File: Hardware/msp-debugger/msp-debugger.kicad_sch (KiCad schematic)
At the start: 18 parts, among them J1 USB_B_Micro, J2 Conn_02x10, J3 Conn_02x10, J4 Conn_01x04_Pin, U1 MSP430G2553IN20, U2 NHD-0420H1Z, U3 BA033CC0FP-E2, U4 FT230XS-R

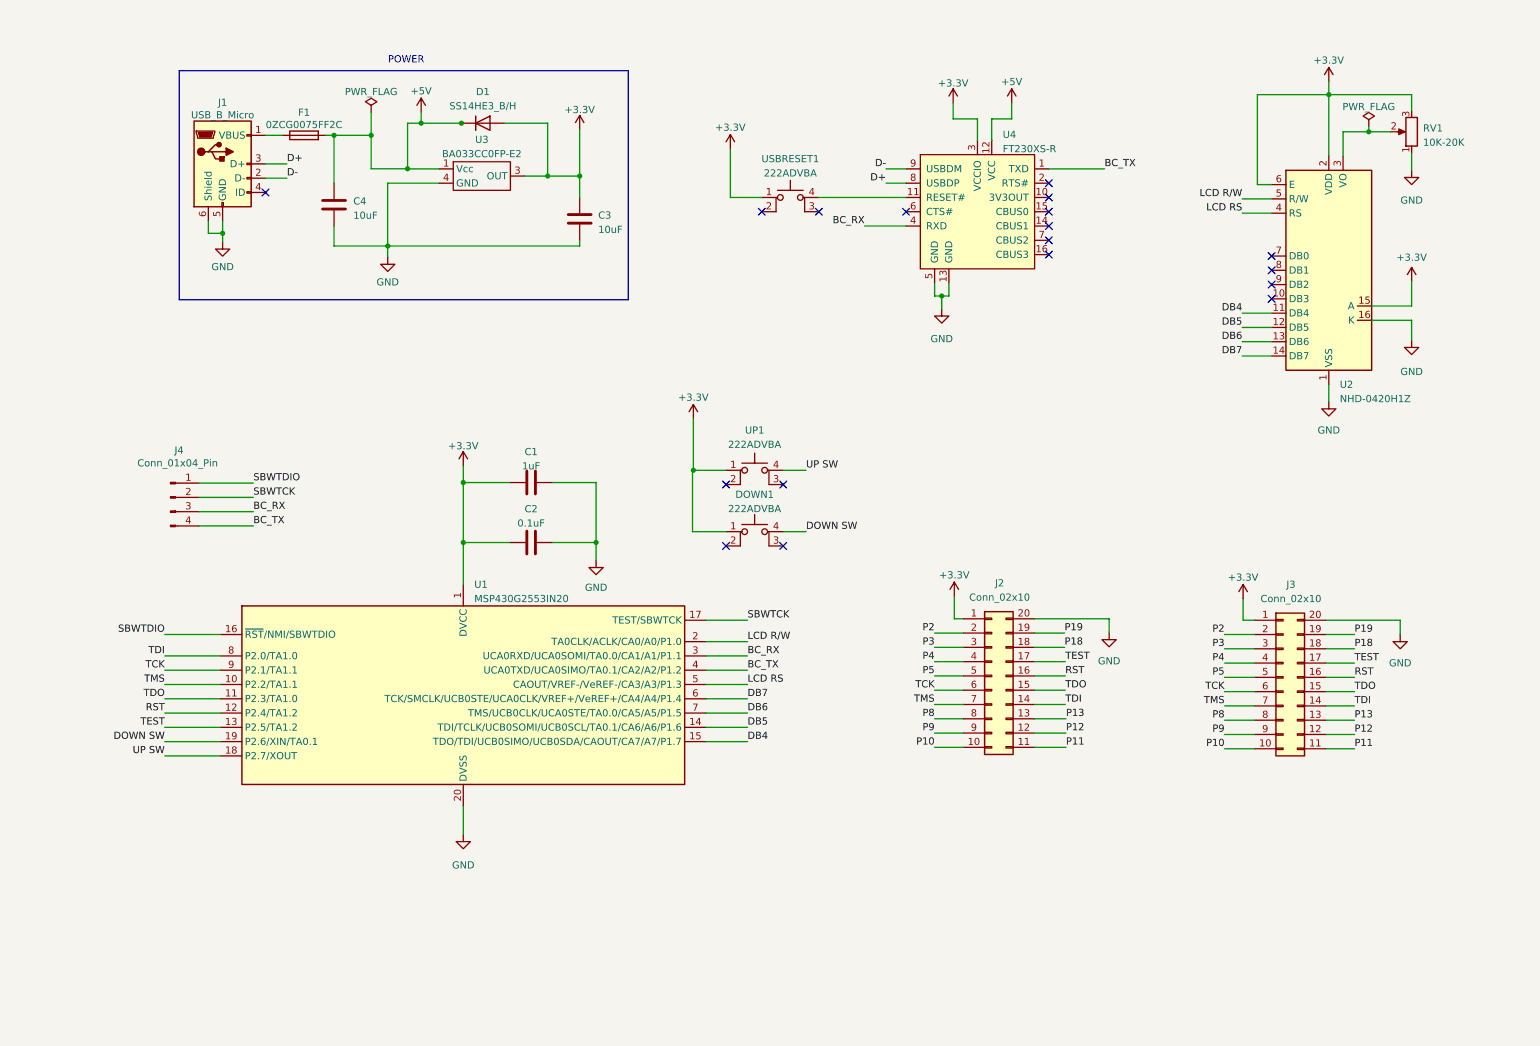
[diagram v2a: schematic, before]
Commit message: update schematic to use length 40 lcd
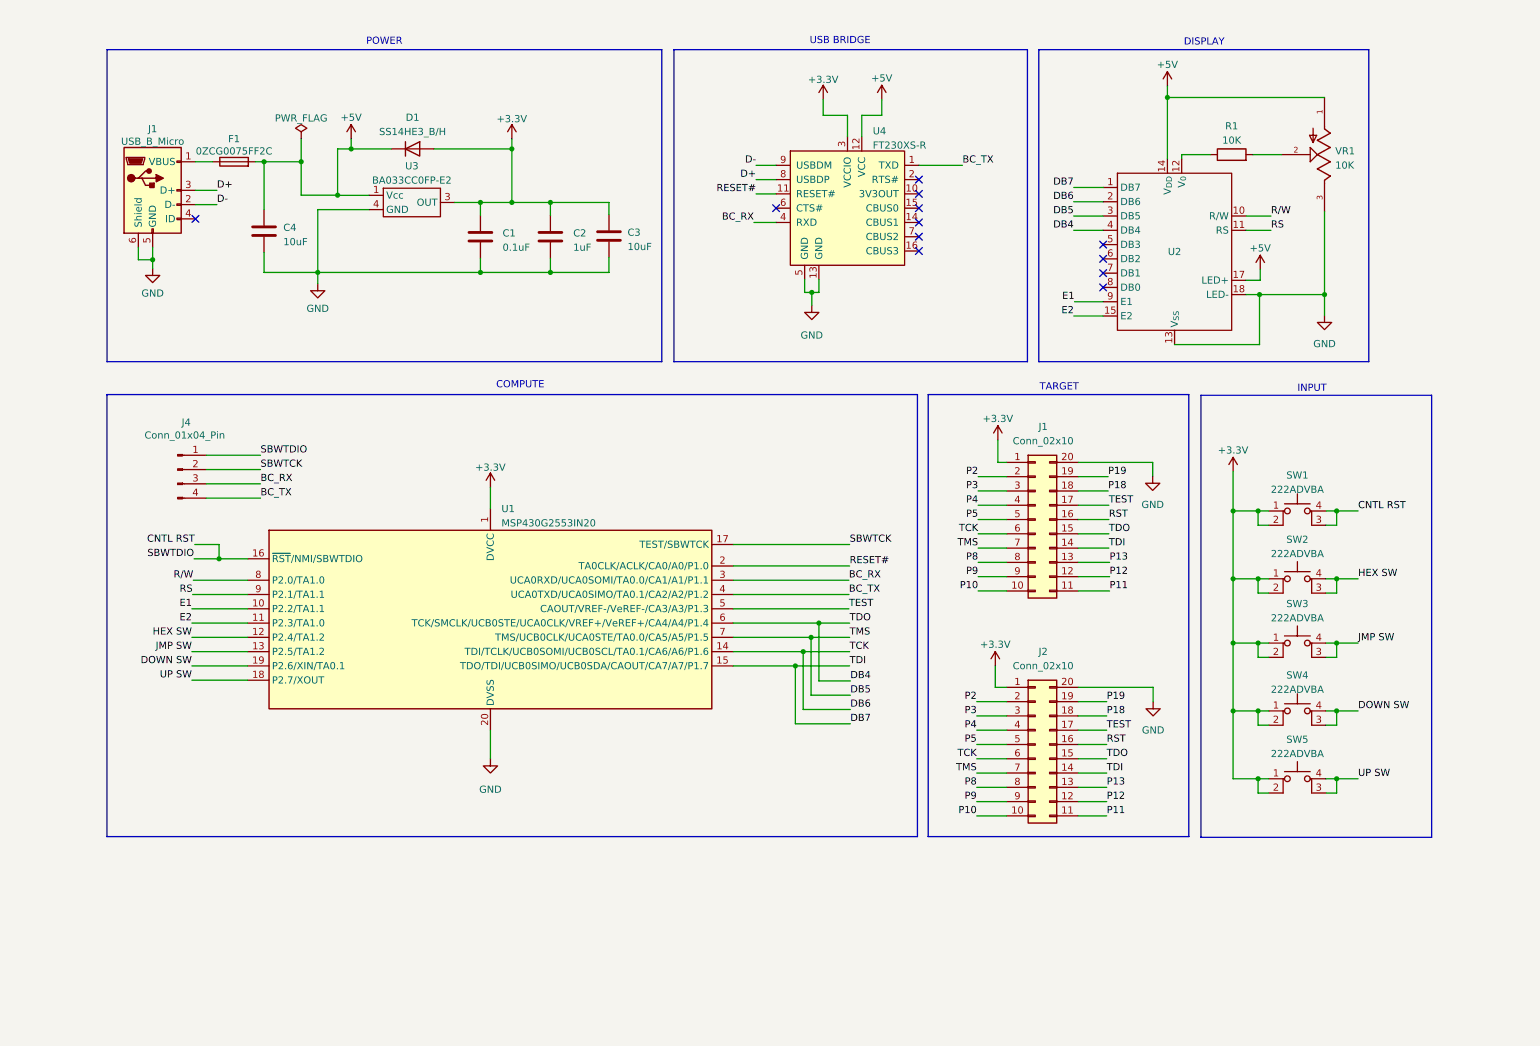
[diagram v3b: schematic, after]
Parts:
- removed C1: 1uF, Capacitor_SMD:C_0805_2012Metric, symbol Device:C
- removed RV1: 10K-20K, project:Potentiometer_CTS_PTN10-E20HB20, symbol Device:R_Potentiometer
- removed U2: NHD-0420H1Z, Display:NHD-0420H1Z, symbol Display_Character:NHD-0420H1Z
- added C2: 1uF, Capacitor_SMD:C_0805_2012Metric, symbol Device:C
- added R1: 10K, symbol Device:R
- added SW4, SW5: 222ADVBA, buttons:SW_222ADVBA, symbol Switch:SW_MEC_5E
- added U2: ~, symbol display:NHD-0440AZ-FL-YBW
- added VR1: 10K, 3362P-1-103LF:TRIM_3362P-1-103LF, symbol ICs:3362P-1-103LF
- renumbered C2 to C1, J2 to J1, J3 to J2, USBRESET1 to SW1, UP1 to SW2, DOWN1 to SW3
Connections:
- net LCD RS is gone; now on net TEST: U1.5 (CAOUT/VREF-/VeREF-/CA3/A3/P1.3)
- net LCD R/W is gone; now on net RESET#: U1.2 (TA0CLK/ACLK/CA0/A0/P1.0)
- net SBWTDIO is gone; now on net CNTL RST: J4.1 (Pin_1), U1.16 (~{RST}/NMI/SBWTDIO)
- net +3.3V: now also C1.2, SW1.2, SW2.2, SW3.2, C2.1, SW4.1, SW4.2, SW5.1, SW5.2; no longer C1.1
- net +5V: now also U2.14 (V_{DD}), U2.17 (LED+), VR1.1
- net DB4: now also J1.15 (Pin_15), J2.15 (Pin_15), U1.6 (TCK/SMCLK/UCB0STE/UCA0CLK/VREF+/VeREF+/CA4/A4/P1.4), U2.4 (DB4); no longer U1.15 (TDO/TDI/UCB0SIMO/UCB0SDA/CAOUT/CA7/A7/P1.7)
- net DB5: now also J1.7 (Pin_7), J2.7 (Pin_7), U1.7 (TMS/UCB0CLK/UCA0STE/TA0.0/CA5/A5/P1.5), U2.3 (DB5); no longer U1.14 (TDI/TCLK/UCB0SOMI/UCB0SCL/TA0.1/CA6/A6/P1.6)
- net DB6: now also J1.6 (Pin_6), J2.6 (Pin_6), U1.14 (TDI/TCLK/UCB0SOMI/UCB0SCL/TA0.1/CA6/A6/P1.6), U2.2 (DB6); no longer U1.7 (TMS/UCB0CLK/UCA0STE/TA0.0/CA5/A5/P1.5)
- net DB7: now also J1.14 (Pin_14), J2.14 (Pin_14), U1.15 (TDO/TDI/UCB0SIMO/UCB0SDA/CAOUT/CA7/A7/P1.7), U2.1 (DB7); no longer U1.6 (TCK/SMCLK/UCB0STE/UCA0CLK/VREF+/VeREF+/CA4/A4/P1.4)
- net DOWN SW: now also SW4.3 (K), SW4.4 (A); no longer SW3.4 (A)
- net GND: now also C1.1, C2.2, U2.13 (V_{SS}), U2.18 (LED-), VR1.3; no longer C1.2
- net RST: no longer U1.12 (P2.4/TA1.2)
- net TEST: no longer U1.13 (P2.5/TA1.2)
- net UP SW: now also SW5.3 (K), SW5.4 (A); no longer SW2.4 (A)
- net HEX SW: now reaches SW2.3 (K)
- net HEX SW: now also SW2.4 (A), U1.12 (P2.4/TA1.2)
- net CNTL RST: now reaches SW1.3 (K)
- net CNTL RST: now also SW1.4 (A)
- net RESET#: now reaches U4.11 (RESET#)
- net RESET#: no longer SW1.4 (A)
- net JMP SW: now reaches SW3.3 (K)
- net JMP SW: now also SW3.4 (A), U1.13 (P2.5/TA1.2)
- removed net TCK: J1.6 (Pin_6), J2.6 (Pin_6), U1.9 (P2.1/TA1.1)
- removed net TDI: J1.14 (Pin_14), J2.14 (Pin_14), U1.8 (P2.0/TA1.0)
- removed net TDO: J1.15 (Pin_15), J2.15 (Pin_15), U1.11 (P2.3/TA1.0)
- removed net TMS: J1.7 (Pin_7), J2.7 (Pin_7), U1.10 (P2.2/TA1.1)
- new net: R1.1, U2.12 (V_{0})
- new net: R1.2, VR1.2
- new net E1: U1.10 (P2.2/TA1.1), U2.9 (E1)
- new net E2: U1.11 (P2.3/TA1.0), U2.15 (E2)
- new net RS: U1.9 (P2.1/TA1.1), U2.11 (RS)
- new net R/W: U1.8 (P2.0/TA1.0), U2.10 (R/W)
- no-connect marks 18 -> 12
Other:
- note added: "COMPUTE"
- note added: "DISPLAY"
- note added: "INPUT"
- note added: "TARGET"
- note added: "USB BRIDGE"
- company: (none) -> Jaden Baptista
- title: (none) -> MSP Debugger
- moved on the sheet: C1, C3, C4, D1, F1, J1, J2, J4, SW1, SW2, SW3, U1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

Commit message: update schematic to active high reset
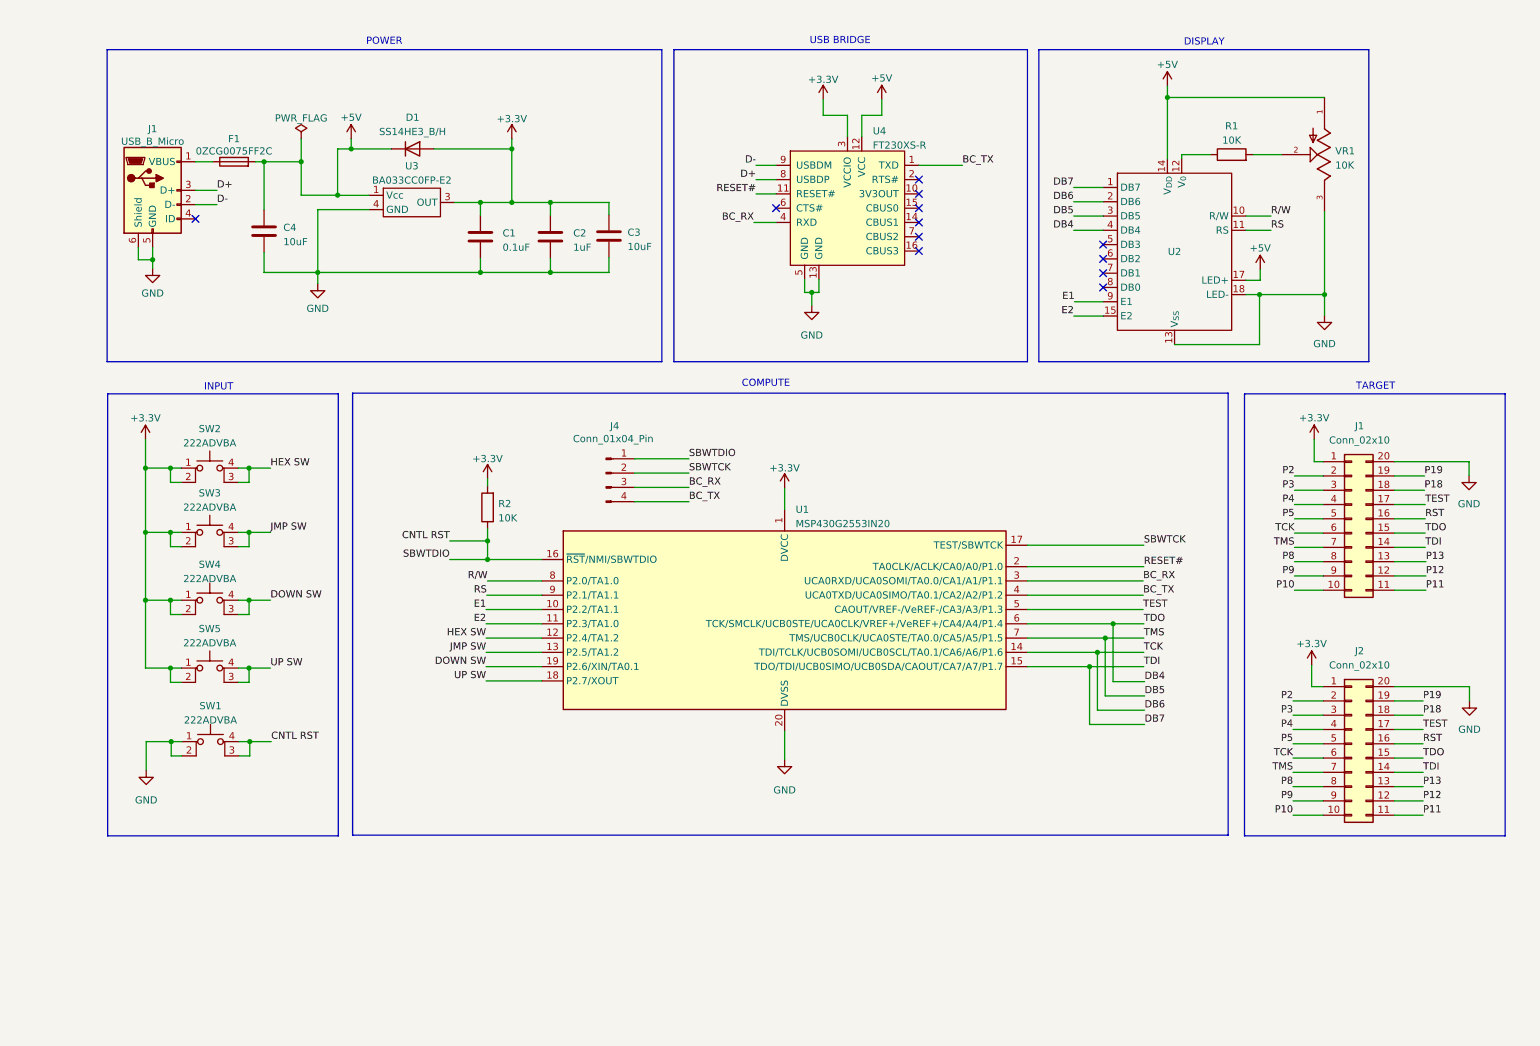
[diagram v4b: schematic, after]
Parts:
- added R2: 10K, Capacitor_SMD:C_0805_2012Metric, symbol Device:R
- R1: footprint (none) -> Capacitor_SMD:C_0805_2012Metric
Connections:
- net +3.3V: now also R2.2; no longer SW1.1, SW1.2
- net CNTL RST: now also R2.1
- net GND: now also SW1.1, SW1.2
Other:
- moved on the sheet: J1, J2, J4, SW1, SW2, SW3, SW4, SW5, U1
